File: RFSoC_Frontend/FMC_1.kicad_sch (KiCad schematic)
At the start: 1 part, among them J10 LPAM-40-01.0-X-08-X-K-TR

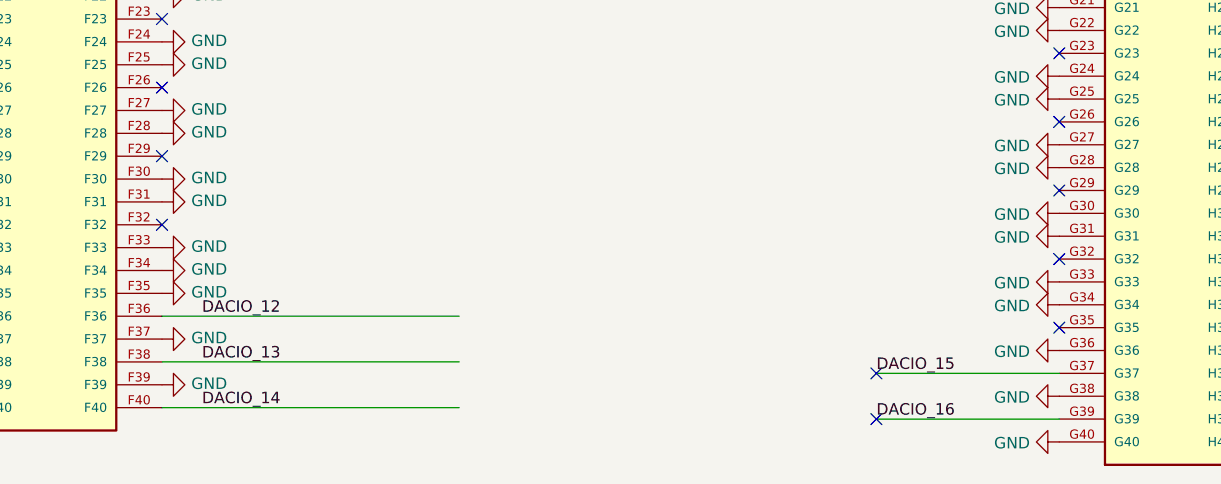
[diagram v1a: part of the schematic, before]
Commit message: fixed grounded util 3v3 pins on the LPAM Cnctr
updated to REV B
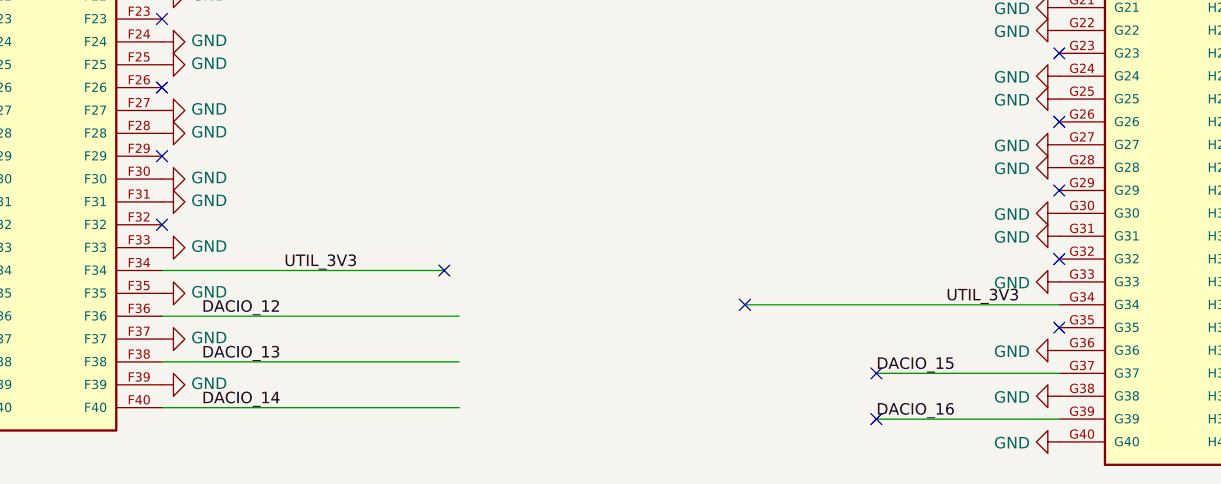
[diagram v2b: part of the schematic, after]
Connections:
- net GND: no longer J10.F34, J10.G34
- net UTIL_3V3: now also J10.F34, J10.G34
- no-connect marks 66 -> 68
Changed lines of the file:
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@@
   (no_connect (at 213.995 132.08))
   (no_connect (at 213.995 127))
+  (no_connect (at 337.439 121.285))
   (no_connect (at 82.55 44.45))
   (no_connect (at 64.77 113.03))
@@
   (no_connect (at 252.095 133.985))
   (no_connect (at 139.7 68.58))
+  (no_connect (at 370.84 125.095))
   (no_connect (at 82.55 59.69))
   (no_connect (at 139.7 38.1))
@@
     (stroke (width 0) (type default) (color 0 0 0 0))
   )
+  (wire (pts (xy 306.07 121.285) (xy 337.439 121.285))
+    (stroke (width 0) (type default) (color 0 0 0 0))
+  )
   (wire (pts (xy 39.37 105.41) (xy 39.37 107.95))
     (stroke (width 0) (type default) (color 0 0 0 0))
@@
     (stroke (width 0) (type default) (color 0 0 0 0))
   )
+  (wire (pts (xy 405.765 125.095) (xy 370.84 125.095))
+    (stroke (width 0) (type default) (color 0 0 0 0))
+  )
   (wire (pts (xy 186.69 106.68) (xy 186.69 109.22))
     (stroke (width 0) (type default) (color 0 0 0 0))
@@
     (effects (font (size 1.27 1.27)) (justify left bottom))
   )
+  (label "UTIL_3V3" (at 319.659 121.285 0)
+    (effects (font (size 1.27 1.27)) (justify left bottom))
+  )
   (label "RFMC_DAC_06_P" (at 141.605 83.82 0)
     (effects (font (size 1.27 1.27)) (justify left bottom))
@@
     (effects (font (size 1.27 1.27)) (justify left bottom))
   )
+  (label "UTIL_3V3" (at 401.32 125.095 180)
+    (effects (font (size 1.27 1.27)) (justify right bottom))
+  )
   (label "VCC12_SW" (at 142.875 38.1 0)
     (effects (font (size 1.27 1.27)) (justify left bottom))
@@
     (pin "1")
   )
-  (symbol (lib_id "power:GND") (at 405.765 125.095 270) (unit 1)
-    (in_bom yes) (on_board yes)
-    (property "Reference" "#PWR0240" (id 0) (at 399.415 125.095 0)
-      (effects (font (size 1.27 1.27)) hide)
-    )
-    (property "Value" "GND" (id 1) (at 402.5138 125.222 90)
-      (effects (font (size 1.27 1.27)) (justify right))
-    )
-    (property "Footprint" "" (id 2) (at 405.765 125.095 0)
-      (effects (font (size 1.27 1.27)) hide)
-    )
-    (property "Datasheet" "" (id 3) (at 405.765 125.095 0)
-      (effects (font (size 1.27 1.27)) hide)
-    )
-    (pin "1")
-  )
   (symbol (lib_id "power:GND") (at 405.765 61.595 270) (unit 1)
     (in_bom yes) (on_board yes)
@@
       (effects (font (size 1.27 1.27)) hide)
     )
-    (pin "1")
-  )
-  (symbol (lib_id "power:GND") (at 306.07 121.285 90) (unit 1)
-    (in_bom yes) (on_board yes)
-    (property "Reference" "#PWR0322" (id 0) (at 312.42 121.285 0)
-      (effects (font (size 1.27 1.27)) hide)
-    )
-    (property "Value" "GND" (id 1) (at 309.3212 121.158 90)
-      (effects (font (size 1.27 1.27)) (justify right))
-    )
-    (property "Footprint" "" (id 2) (at 306.07 121.285 0)
-      (effects (font (size 1.27 1.27)) hide)
-    )
-    (property "Datasheet" "" (id 3) (at 306.07 121.285 0)
-      (effects (font (size 1.27 1.27)) hide)
-    )
